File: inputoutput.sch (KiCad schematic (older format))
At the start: 20 parts, among them J2 TimerCounter, J3 GPIO1, J4 GPIO2, J5 PS/2 Keyboard, J6 RS232, Q1 2N3904, Q2 2N3904, U11 Z84C30-CTC, U12 Z84C40-SIO-0, U14 Z84C200-PIO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

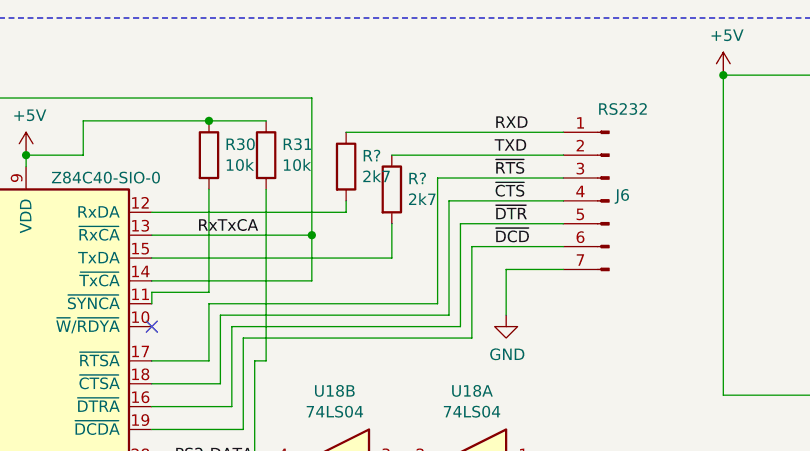
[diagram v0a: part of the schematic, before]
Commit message: Added RTC voltage detection circuit
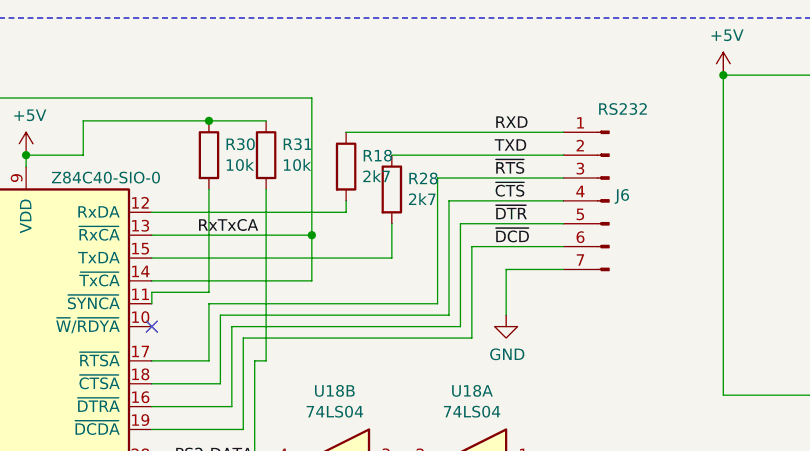
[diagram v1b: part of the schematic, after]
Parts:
- gave numbers to parts that had none: 2
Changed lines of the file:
@@
 encoding utf-8
 Sheet 3 6
-Title "Z80 Computer / Input & Output"
-Date "2021-02-02"
-Rev "2"
+Title "Z80 Computer"
+Date "2021-05-04"
+Rev "3"
 Comp "Jaap Geurts"
 Comment1 ""
@@
 NoConn ~ 10600 1950
 $Comp
-L Device:R R?
+L Device:R R18
 U 1 1 60A95CDC
 P 7100 1500
-F 0 "R?" H 7170 1546 50  0000 L CNN
+F 0 "R18" H 7170 1546 50  0000 L CNN
 F 1 "2k7" H 7170 1455 50  0000 L CNN
 F 2 "" V 7030 1500 50  0001 C CNN
@@
 	7100 1350 8050 1350
 $Comp
-L Device:R R?
+L Device:R R28
 U 1 1 60AE8D9E
 P 7300 1600
-F 0 "R?" H 7370 1646 50  0000 L CNN
+F 0 "R28" H 7370 1646 50  0000 L CNN
 F 1 "2k7" H 7370 1555 50  0000 L CNN
 F 2 "" V 7230 1600 50  0001 C CNN
